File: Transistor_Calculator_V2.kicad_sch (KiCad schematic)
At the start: 51 parts, among them Q1 2N3904, Q10 2N3904, Q11 2N3904, Q12 2N3904, Q13 2N3904, Q14 2N3904, Q15 2N3904, Q16 2N3904, Q17 2N3904, Q18 2N3904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

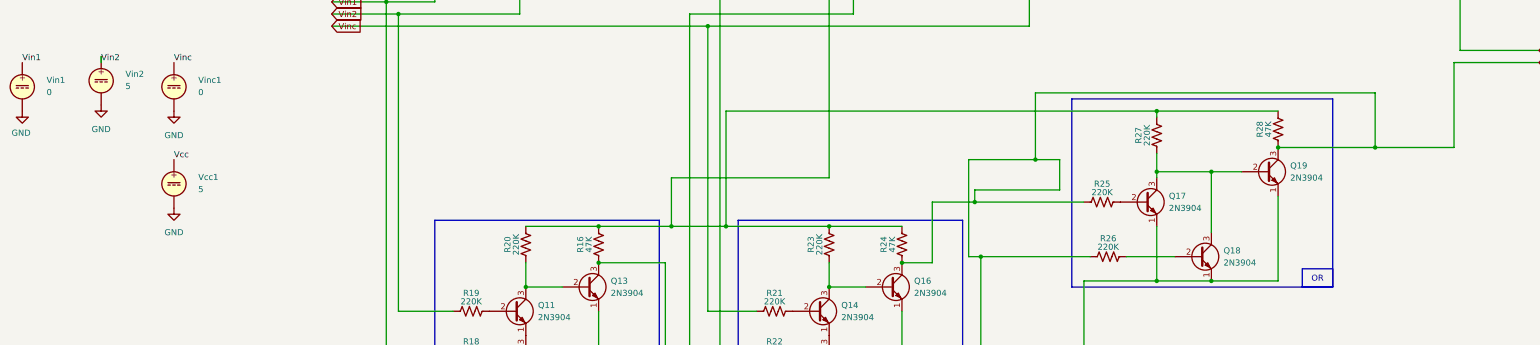
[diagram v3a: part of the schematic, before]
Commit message: Removed the part that was breaking it.
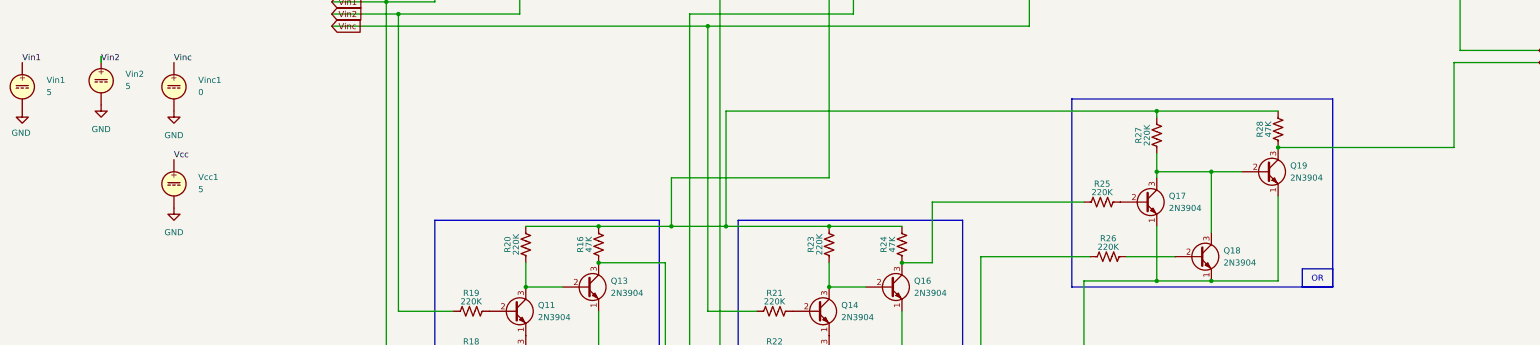
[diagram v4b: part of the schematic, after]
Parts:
- Vin1: value 0 -> 5
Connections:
- net Vo2: no longer Q13.3 (C), Q16.3 (C), R16.1, R24.1, R25.1, R26.1
- new net: Q16.3 (C), R24.1, R25.1
- new net: Q13.3 (C), R16.1, R26.1
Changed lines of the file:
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@@
 	)
 	(junction
-		(at 152.4 144.78)
-		(diameter 0)
-		(color 0 0 0 0)
-	)
-	(junction
 		(at 127 72.39)
 		(diameter 0)
@@
 	)
 	(junction
-		(at 165.1 135.89)
-		(diameter 0)
-		(color 0 0 0 0)
-	)
-	(junction
 		(at 121.92 149.86)
 		(diameter 0)
@@
 	)
 	(junction
-		(at 153.67 156.21)
-		(diameter 0)
-		(color 0 0 0 0)
-	)
-	(junction
 		(at 198.12 31.75)
 		(diameter 0)
@@
 	)
 	(junction
-		(at 236.22 133.35)
-		(diameter 0)
-		(color 0 0 0 0)
-	)
-	(junction
 		(at 91.44 39.37)
 		(diameter 0)
@@
 	(wire
 		(pts
-			(xy 152.4 144.78) (xy 152.4 142.24)
-		)
-		(stroke
-			(width 0)
-			(type default)
-		)
-	)
-	(wire
-		(pts
 			(xy 107.95 85.09) (xy 161.29 85.09)
 		)
@@
 	(wire
 		(pts
-			(xy 165.1 121.92) (xy 165.1 135.89)
-		)
-		(stroke
-			(width 0)
-			(type default)
-		)
-	)
-	(wire
-		(pts
-			(xy 143.51 144.78) (xy 152.4 144.78)
-		)
-		(stroke
-			(width 0)
-			(type default)
-		)
-	)
-	(wire
-		(pts
-			(xy 165.1 121.92) (xy 236.22 121.92)
+			(xy 143.51 144.78) (xy 175.26 144.78)
 		)
 		(stroke
@@
 	(wire
 		(pts
-			(xy 170.18 142.24) (xy 170.18 135.89)
-		)
-		(stroke
-			(width 0)
-			(type default)
-		)
-	)
-	(wire
-		(pts
 			(xy 252.73 115.57) (xy 252.73 133.35)
 		)
@@
 	(wire
 		(pts
-			(xy 236.22 121.92) (xy 236.22 133.35)
-		)
-		(stroke
-			(width 0)
-			(type default)
-		)
-	)
-	(wire
-		(pts
 			(xy 190.5 134.62) (xy 190.5 138.43)
 		)
@@
 	(wire
 		(pts
-			(xy 236.22 133.35) (xy 252.73 133.35)
-		)
-		(stroke
-			(width 0)
-			(type default)
-		)
-	)
-	(wire
-		(pts
 			(xy 121.92 182.88) (xy 121.92 191.77)
 		)
@@
 	(wire
 		(pts
-			(xy 151.13 156.21) (xy 151.13 135.89)
-		)
-		(stroke
-			(width 0)
-			(type default)
-		)
-	)
-	(wire
-		(pts
 			(xy 198.12 39.37) (xy 198.12 54.61)
 		)
@@
 	(wire
 		(pts
-			(xy 165.1 135.89) (xy 170.18 135.89)
-		)
-		(stroke
-			(width 0)
-			(type default)
-		)
-	)
-	(wire
-		(pts
 			(xy 17.78 102.87) (xy 29.21 102.87)
 		)
@@
 	(wire
 		(pts
-			(xy 215.9 133.35) (xy 236.22 133.35)
+			(xy 215.9 133.35) (xy 252.73 133.35)
 		)
 		(stroke
@@
 	(wire
 		(pts
-			(xy 153.67 156.21) (xy 151.13 156.21)
-		)
-		(stroke
-			(width 0)
-			(type default)
-		)
-	)
-	(wire
-		(pts
 			(xy 180.34 38.1) (xy 180.34 39.37)
 		)
@@
 	(wire
 		(pts
-			(xy 151.13 135.89) (xy 165.1 135.89)
-		)
-		(stroke
-			(width 0)
-			(type default)
-		)
-	)
-	(wire
-		(pts
 			(xy 207.01 44.45) (xy 207.01 39.37)
 		)
@@
 	(wire
 		(pts
-			(xy 152.4 144.78) (xy 175.26 144.78)
-		)
-		(stroke
-			(width 0)
-			(type default)
-		)
-	)
-	(wire
-		(pts
 			(xy 161.29 85.09) (xy 179.07 85.09)
 		)
@@
 	(wire
 		(pts
-			(xy 152.4 142.24) (xy 170.18 142.24)
-		)
-		(stroke
-			(width 0)
-			(type default)
-		)
-	)
-	(wire
-		(pts
 			(xy 148.59 43.18) (xy 171.45 43.18)
 		)
@@
 			)
 		)
-		(property "Value" "0"
+		(property "Value" "5"
 			(at -41.91 121.7901 0)
 			(effects
